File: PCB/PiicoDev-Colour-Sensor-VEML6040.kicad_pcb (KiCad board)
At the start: 2 copper layers, 25.4 x 25.4 mm, 19 parts, among them J1 , J2 , J3 Conn_PiicoDev_header_01x04_Ma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, U1 VEML6040

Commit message: Replace power LED with illumination LED
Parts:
- added J4: Conn_01x01_Male, CoreElectronics_Components:PiicoDev_header_1pin_LED, B.Cu at (17.8, 24.1)
- added Q1: BSS138, Package_TO_SOT_SMD:SOT-23, F.Cu at (17.0, 10.2)
- added R2: 10k, Resistor_SMD:R_0402_1005Metric, F.Cu at (23.1, 18.3)
- D1: value LED -> LED 5000K; footprint LED_SMD:LED_0603_1608Metric -> CoreElectronics_Components:LED_1208_3020Metric_Heatsink
- R1: value 1k -> 68R
- moved D1 7.25 mm to (12.7, 9.14)
- moved J3 1.27 mm to (7.62, 24.1)
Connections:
- D1 pad 1: GND -> Net-(D1-Pad1)
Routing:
- net /LED_EN: track 0.00 -> 20.4 mm
- net +3V3: track 39.0 -> 51.8 mm, vias 2 -> 4
- net Net-(D1-Pad2): track 1.24 -> 8.32 mm
- net Net-(D1-Pad1): track 0.00 -> 2.70 mm
- net GND: track 9.61 -> 7.55 mm, vias 3 -> 4
- net /SDA: track 51.9 -> 50.7 mm
- net /SCL: track 43.1 -> 44.1 mm
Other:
- board text added: "LED"
- board text added: "v01"
- board text removed: "PWR LED"
- board text removed: "v00"

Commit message: Tweak layout
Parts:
- moved R1 5.76 mm to (8.63, 9.14)
- moved Q1 0.51 mm to (17.0, 9.65)
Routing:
- net Net-(D1-Pad2): track 8.32 -> 2.16 mm
- net Net-(JP1-Pad2): track 3.46 -> 6.57 mm

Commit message: Update version number
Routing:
- net GND: vias 4 -> 5
- added copper zone on F.Cu, net GND
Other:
- board text added: "v10"
- board text removed: "v01"
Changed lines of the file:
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@@
-(kicad_pcb (version 20171130) (host pcbnew "(5.1.9)-1")
+(kicad_pcb (version 20171130) (host pcbnew "(5.1.10)-1")
   (general
     (thickness 1.6)
     (drawings 44)
-    (tracks 112)
+    (tracks 113)
     (zones 0)
     (modules 22)
@@
     (effects (font (size 1 1) (thickness 0.2)) (justify mirror))
   )
-  (gr_text v01 (at 3.683 23.9395) (layer B.Cu)
+  (gr_text v10 (at 3.683 23.9395) (layer B.Cu)
     (effects (font (size 1 1) (thickness 0.2)) (justify left mirror))
   )
@@
   (segment (start 18.73 8.702) (end 19.304 8.128) (width 0.25) (layer F.Cu) (net 2))
   (segment (start 18.018 8.702) (end 18.73 8.702) (width 0.25) (layer F.Cu) (net 2))
+  (via (at 22.7 22.7) (size 0.8) (drill 0.4) (layers F.Cu B.Cu) (net 2))
   (segment (start 9.144 9.144) (end 11.3 9.144) (width 0.25) (layer F.Cu) (net 3))
   (segment (start 6.58 14.2) (end 5.2766 14.2) (width 0.25) (layer F.Cu) (net 4) (status 20))
@@
       )
     )
+  )
+  (zone (net 2) (net_name GND) (layer F.Cu) (hatch edge 0.508)
+    (connect_pads (clearance 0.508))
+    (min_thickness 0.254)
+    (fill yes (arc_segments 32) (thermal_gap 0.508) (thermal_bridge_width 0.508))
+    (polygon
+      (pts
+        (xy 25.4 25.4) (xy 0 25.4) (xy 0 0) (xy 25.4 0)
+      )
+    )

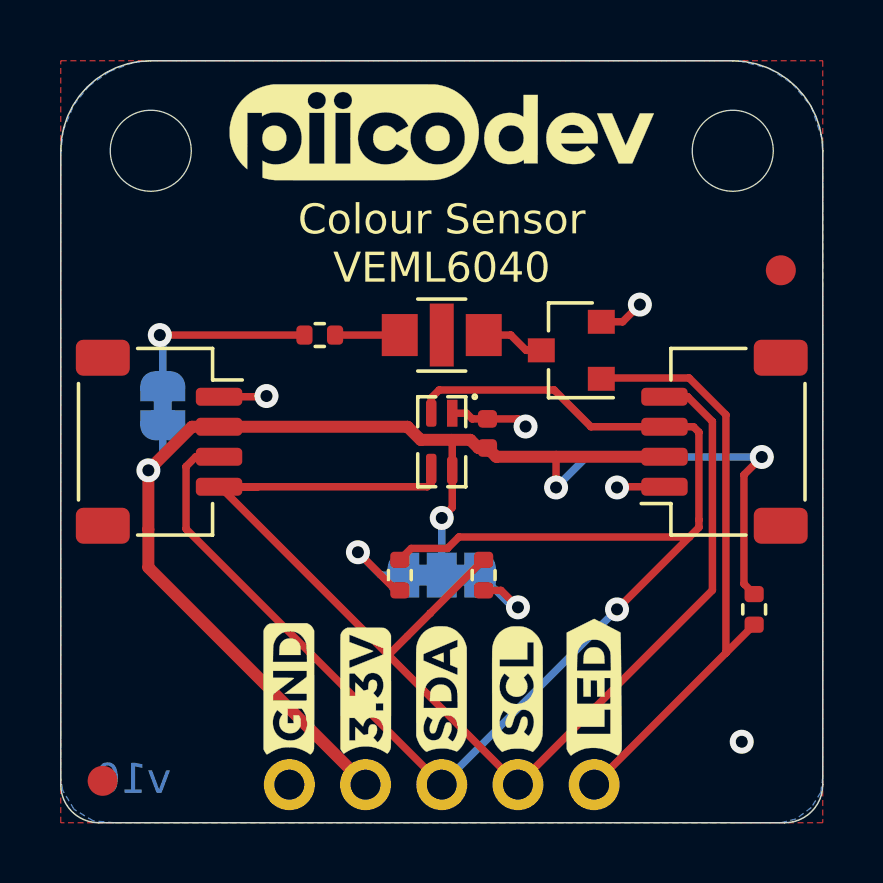
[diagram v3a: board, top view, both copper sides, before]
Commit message: Add LED bypass resistor
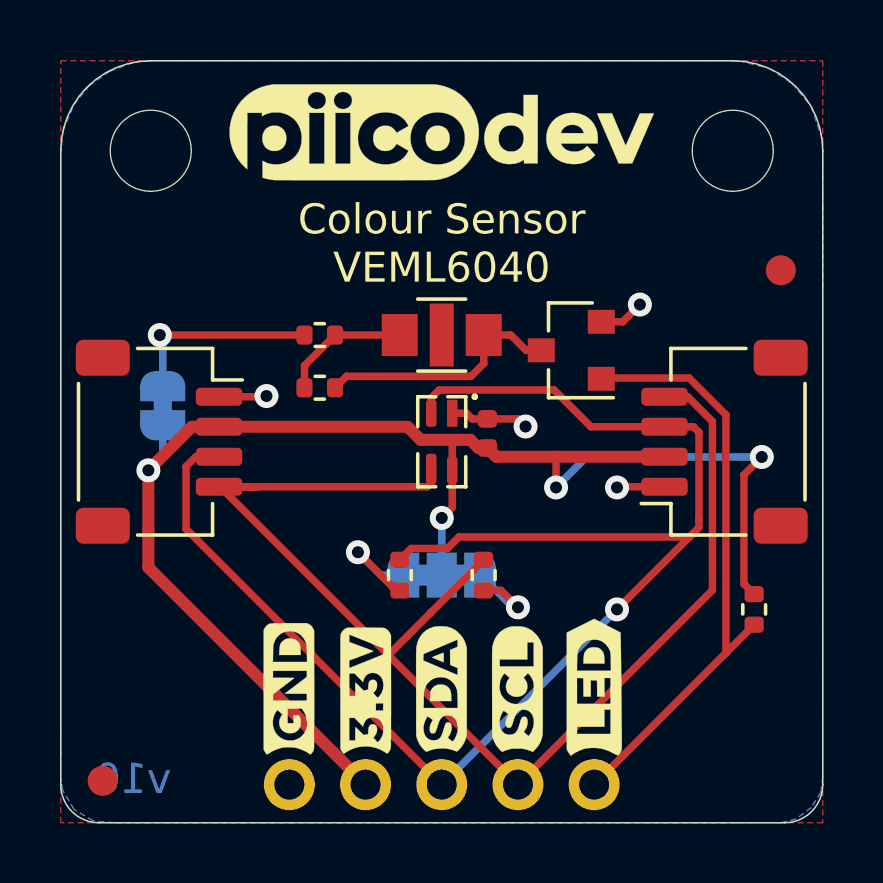
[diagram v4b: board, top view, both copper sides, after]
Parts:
- added R5: 4.7k, Resistor_SMD:R_0402_1005Metric, F.Cu at (8.63, 10.9)
- R2: value 10k -> 4.7k
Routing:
- net Net-(D1-Pad1): track 2.49 -> 8.73 mm
- net Net-(D1-Pad2): track 2.16 -> 4.33 mm
- net GND: vias 5 -> 4
- added copper zone on F.Cu, net (none)
- removed copper zone on F.Cu, net GND
